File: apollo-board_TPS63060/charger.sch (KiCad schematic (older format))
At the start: 31 parts, among them J4 DNP/JST_ZH_S2B_thru, J5 DNP/JST_XH_S2B_thru, Q12 DMP2035UVT, Q15 DMN3023L, Q3 DMN3023L, Q4 2N7002A, U4 LTC4162EUFD-LAD

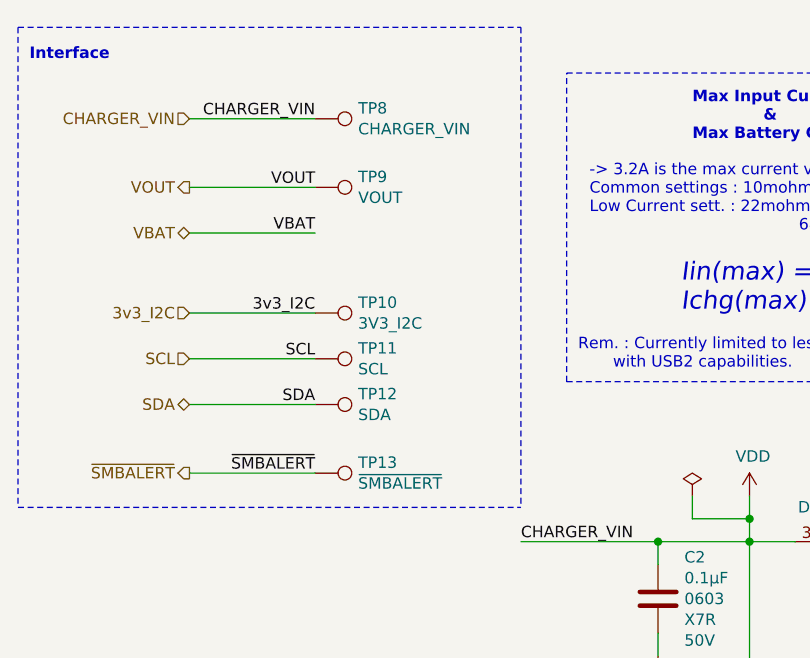
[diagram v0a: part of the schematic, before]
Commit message: Remove unused parts at schematic level.
+ solve schematic DRC issues
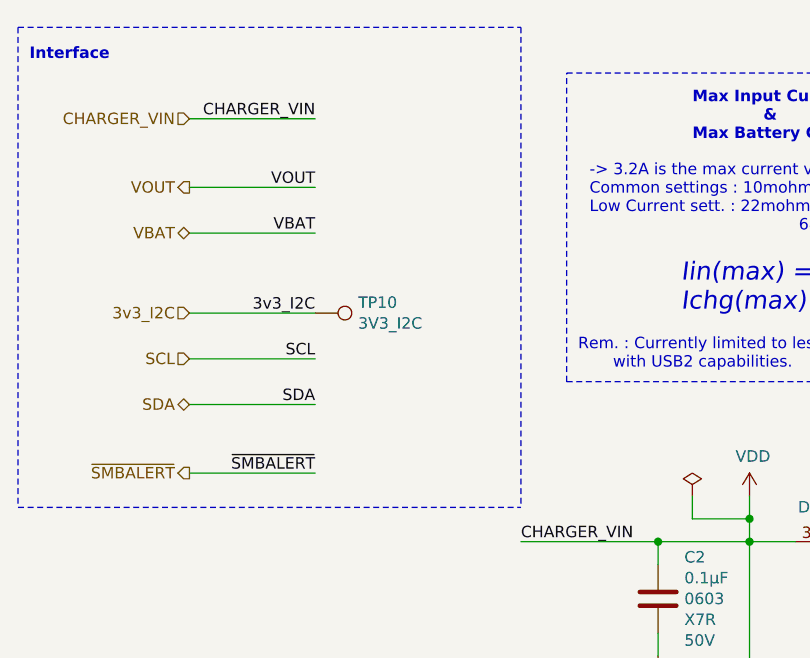
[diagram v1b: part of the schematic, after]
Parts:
- removed TP11: SCL, TestPoint:TestPoint_Pad_D1.0mm, symbol Connector:TestPoint
- removed TP12: SDA, TestPoint:TestPoint_Pad_D1.0mm, symbol Connector:TestPoint
- removed TP13: ~SMBALERT, TestPoint:TestPoint_Pad_D1.0mm, symbol Connector:TestPoint
- removed TP8: CHARGER_VIN, TestPoint:TestPoint_Pad_D1.0mm, symbol Connector:TestPoint
- removed TP9: VOUT, TestPoint:TestPoint_Pad_D1.0mm, symbol Connector:TestPoint
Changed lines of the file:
@@
 	550  550  2750 550
-$Comp
-L Connector:TestPoint TP8
-U 1 1 5FD90BDE
-P 1850 950
-F 0 "TP8" V 1804 1138 50  0000 L CNN
-F 1 "CHARGER_VIN" V 1895 1138 50  0000 L CNN
-F 2 "TestPoint:TestPoint_Pad_D1.0mm" H 2050 950 50  0001 C CNN
-F 3 "~" H 2050 950 50  0001 C CNN
-	1    1850 950
-	0    1    1    0
-$EndComp
-$Comp
-L Connector:TestPoint TP9
-U 1 1 5FD91067
-P 1850 1250
-F 0 "TP9" V 1804 1438 50  0000 L CNN
-F 1 "VOUT" V 1895 1438 50  0000 L CNN
-F 2 "TestPoint:TestPoint_Pad_D1.0mm" H 2050 1250 50  0001 C CNN
-F 3 "~" H 2050 1250 50  0001 C CNN
-	1    1850 1250
-	0    1    1    0
-$EndComp
 $Comp
 L Connector:TestPoint TP10
@@
 	0    1    1    0
 $EndComp
-$Comp
-L Connector:TestPoint TP11
-U 1 1 5FD91A28
-P 1850 2000
-F 0 "TP11" V 1804 2188 50  0000 L CNN
-F 1 "SCL" V 1895 2188 50  0000 L CNN
-F 2 "TestPoint:TestPoint_Pad_D1.0mm" H 2050 2000 50  0001 C CNN
-F 3 "~" H 2050 2000 50  0001 C CNN
-	1    1850 2000
-	0    1    1    0
-$EndComp
-$Comp
-L Connector:TestPoint TP12
-U 1 1 5FD91C9F
-P 1850 2200
-F 0 "TP12" V 1804 2388 50  0000 L CNN
-F 1 "SDA" V 1895 2388 50  0000 L CNN
-F 2 "TestPoint:TestPoint_Pad_D1.0mm" H 2050 2200 50  0001 C CNN
-F 3 "~" H 2050 2200 50  0001 C CNN
-	1    1850 2200
-	0    1    1    0
-$EndComp
-$Comp
-L Connector:TestPoint TP13
-U 1 1 5FD91E2F
-P 1850 2500
-F 0 "TP13" V 1804 2688 50  0000 L CNN
-F 1 "~SMBALERT" V 1895 2688 50  0000 L CNN
-F 2 "TestPoint:TestPoint_Pad_D1.0mm" H 2050 2500 50  0001 C CNN
-F 3 "~" H 2050 2500 50  0001 C CNN
-	1    1850 2500
-	0    1    1    0
-$EndComp

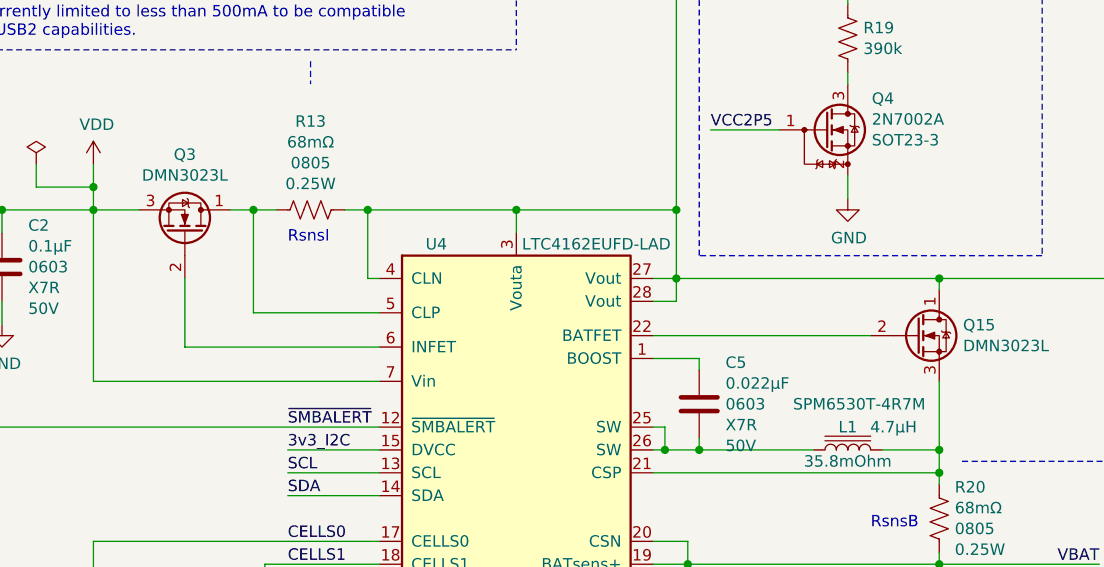
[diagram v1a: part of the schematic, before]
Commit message: Swapped Q3 and Q15 Symbol + Footprint
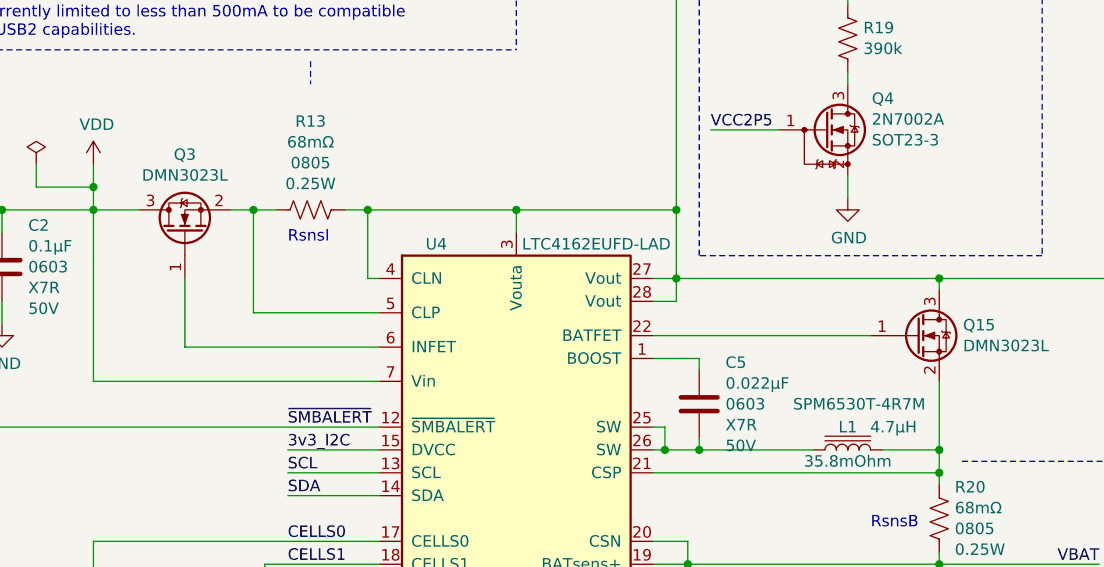
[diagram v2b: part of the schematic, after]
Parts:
- removed Q15, Q3: DMN3023L, Package_TO_SOT_SMD:SOT-23, symbol Device:Q_NMOS_DGS
- added Q15, Q3: DMN3023L, Package_TO_SOT_SMD:SOT-23, symbol Device:Q_NMOS_GSD
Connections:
- net VCC: now also Q15.3 (D)
- net VDD: now also Q3.3 (D)
- net at L1.2, R20.2, U4.21 (CSP): now also Q15.2 (S)
- net at U4.22 (BATFET): now also Q15.1 (G)
- net at R13.2, U4.5 (CLP): now also Q3.2 (S)
- net at U4.6 (INFET): now also Q3.1 (G)
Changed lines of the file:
@@
-	1    0    0    -1
-$EndComp
-$Comp
-L Device:Q_NMOS_DGS Q15
-U 1 1 60069647
-P 7350 3350
-F 0 "Q15" H 7554 3396 50  0000 L CNN
-F 1 "DMN3023L" H 7554 3305 50  0000 L CNN
-F 2 "Package_TO_SOT_SMD:SOT-23" H 7550 3450 50  0001 C CNN
-F 3 "~" H 7350 3350 50  0001 C CNN
-	1    7350 3350
 	1    0    0    -1
 $EndComp
@@
 Wire Wire Line
 	7450 3100 8300 3100
+Text Label 9850 5850 0    50   ~ 0
+VBAT
 $Comp
-L Device:Q_NMOS_DGS Q3
-U 1 1 60066FDA
+L Device:Q_NMOS_GSD Q3
+U 1 1 60CC1585
 P 4150 2900
 F 0 "Q3" V 4492 2900 50  0000 C CNN
@@
 F 3 "~" H 4150 2900 50  0001 C CNN
 	1    4150 2900
-	0    1    -1   0
+	0    -1   -1   0
 $EndComp
-Text Label 9850 5850 0    50   ~ 0
-VBAT
+$Comp
+L Device:Q_NMOS_GSD Q15
+U 1 1 60CC30D9
+P 7350 3350
+F 0 "Q15" H 7554 3396 50  0000 L CNN
+F 1 "DMN3023L" H 7554 3305 50  0000 L CNN
+F 2 "Package_TO_SOT_SMD:SOT-23" H 7550 3450 50  0001 C CNN
+F 3 "~" H 7350 3350 50  0001 C CNN
+	1    7350 3350
+	1    0    0    -1
+$EndComp
 $EndSCHEMATC

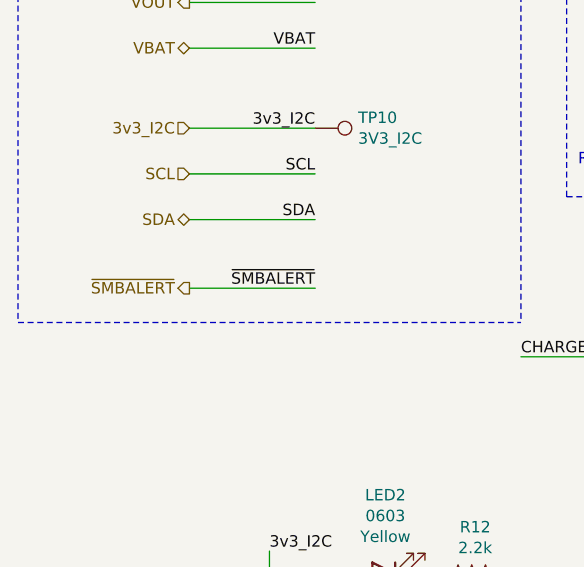
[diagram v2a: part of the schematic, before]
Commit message: Remove SMBALERT wire
between LTC4162-L chip (pin12) and the 2.54mm pitch 13pin connector (pin13). It will allow to use this pin for "one wire" RGB LED (RGB LED Out)
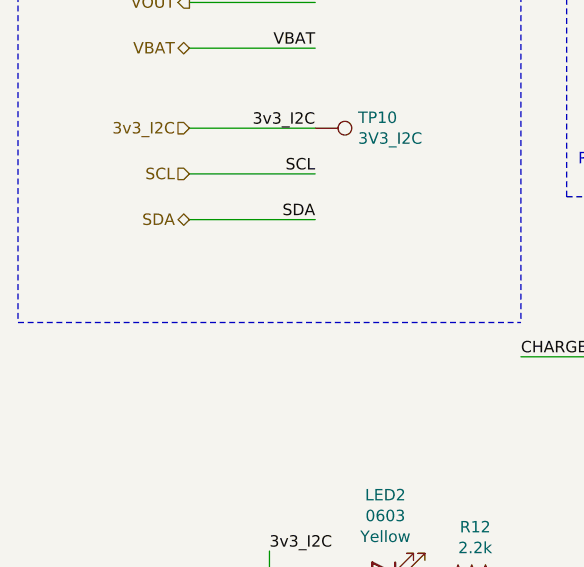
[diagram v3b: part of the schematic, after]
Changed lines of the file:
@@
 Text Label 4600 3750 0    50   ~ 0
-~SMBALERT
-Text HLabel 1300 2500 0    50   Output ~ 0
-~SMBALERT
-Wire Wire Line
-	1850 2500 1300 2500
-Text Label 1850 2500 2    50   ~ 0
 ~SMBALERT
 Text Notes 3000 2050 0    50   ~ 0

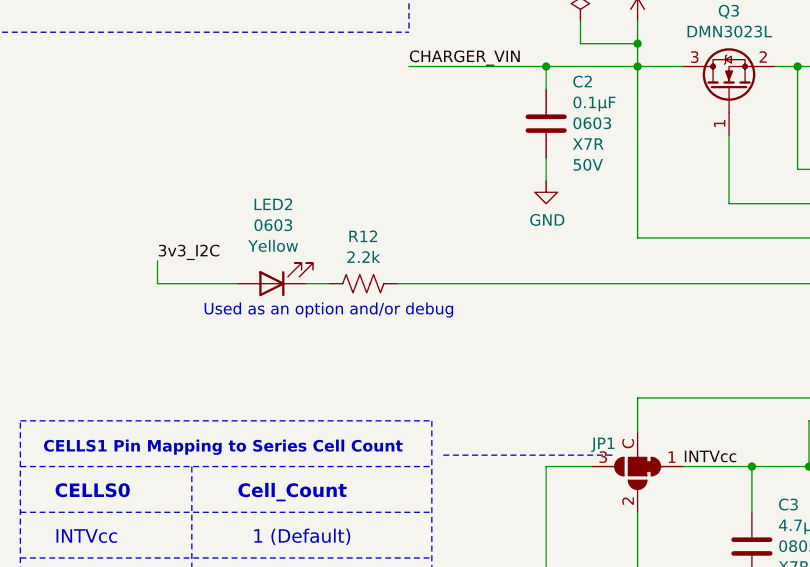
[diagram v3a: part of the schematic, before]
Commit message: Update SMBALERT LED (LED2) and resistor (R12) to DNP (Do Not Populate)
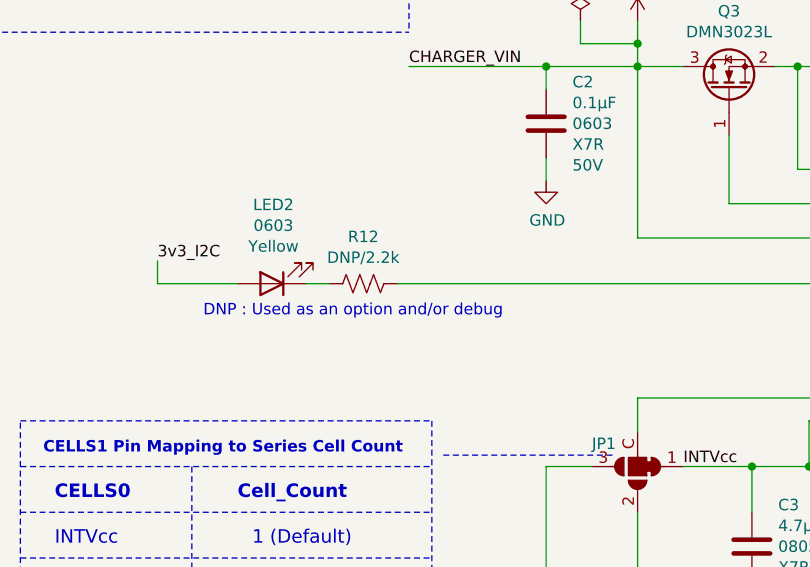
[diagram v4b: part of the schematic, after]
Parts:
- R12: value 2.2k -> DNP/2.2k
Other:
- note added: "DNP : Used as an option and/or debug"
- note removed: "Used as an option and/or debug"
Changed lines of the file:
@@
 P 2550 3750
 F 0 "R12" V 2345 3750 50  0000 C CNN
-F 1 "2.2k" V 2436 3750 50  0000 C CNN
+F 1 "DNP/2.2k" V 2436 3750 50  0000 C CNN
 F 2 "Resistor_SMD:R_0603_1608Metric" V 2590 3740 50  0001 C CNN
 F 3 "~" H 2550 3750 50  0001 C CNN
@@
 	1650 3750 1650 3650
 Text Notes 1850 3900 0    50   ~ 0
-Used as an option and/or debug
+DNP : Used as an option and/or debug
 Wire Wire Line
 	5950 850  6300 850
